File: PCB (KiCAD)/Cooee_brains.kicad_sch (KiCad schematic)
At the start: 35 parts, among them J1 USB4105-GF-A, J2 Conn_Coaxial, J3 503398-1892, J4 Conn_01x14_Socket, J5 Conn_02x20_Counter_Clockwise, J6 Conn_Coaxial, J7 Conn_01x04_Pin, J8 503480-1800, J9 Conn_01x18_Socket, SW1 Prog, SW2 Reset, U1 AMS1117-3.3, U2 ESP32-S3-WROOM-1-N8, U3 MAX98357AETE_T, U4 SX1262IMLTRT

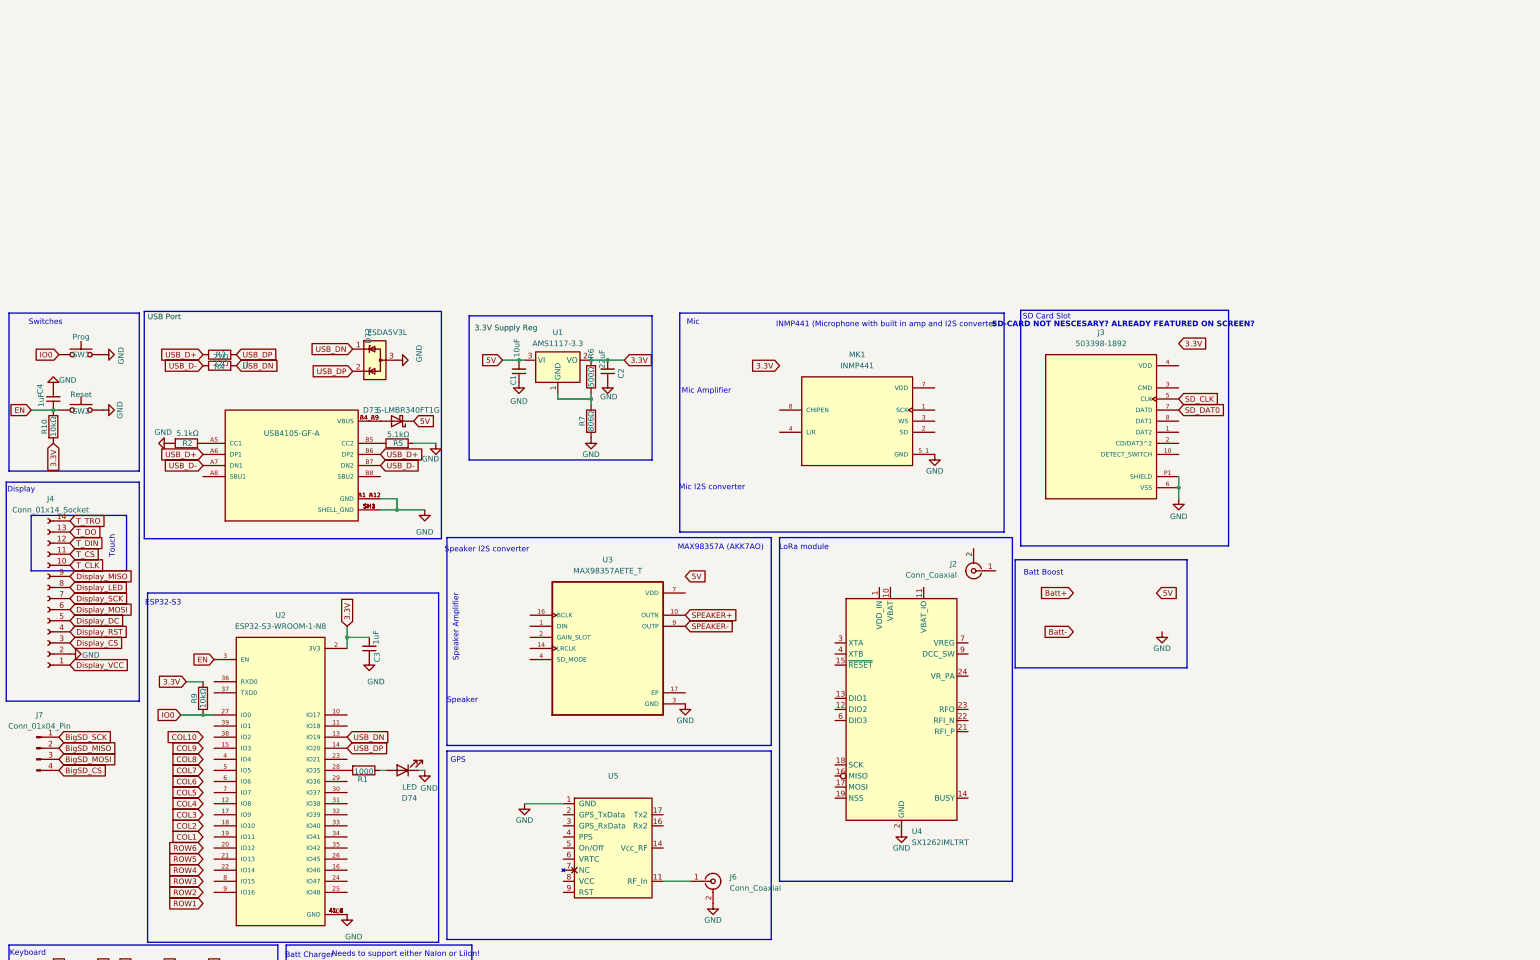
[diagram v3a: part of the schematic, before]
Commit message: swapped out complex SX1262 circuitry for a module
swapped out complex SX1262 circuitry for a module
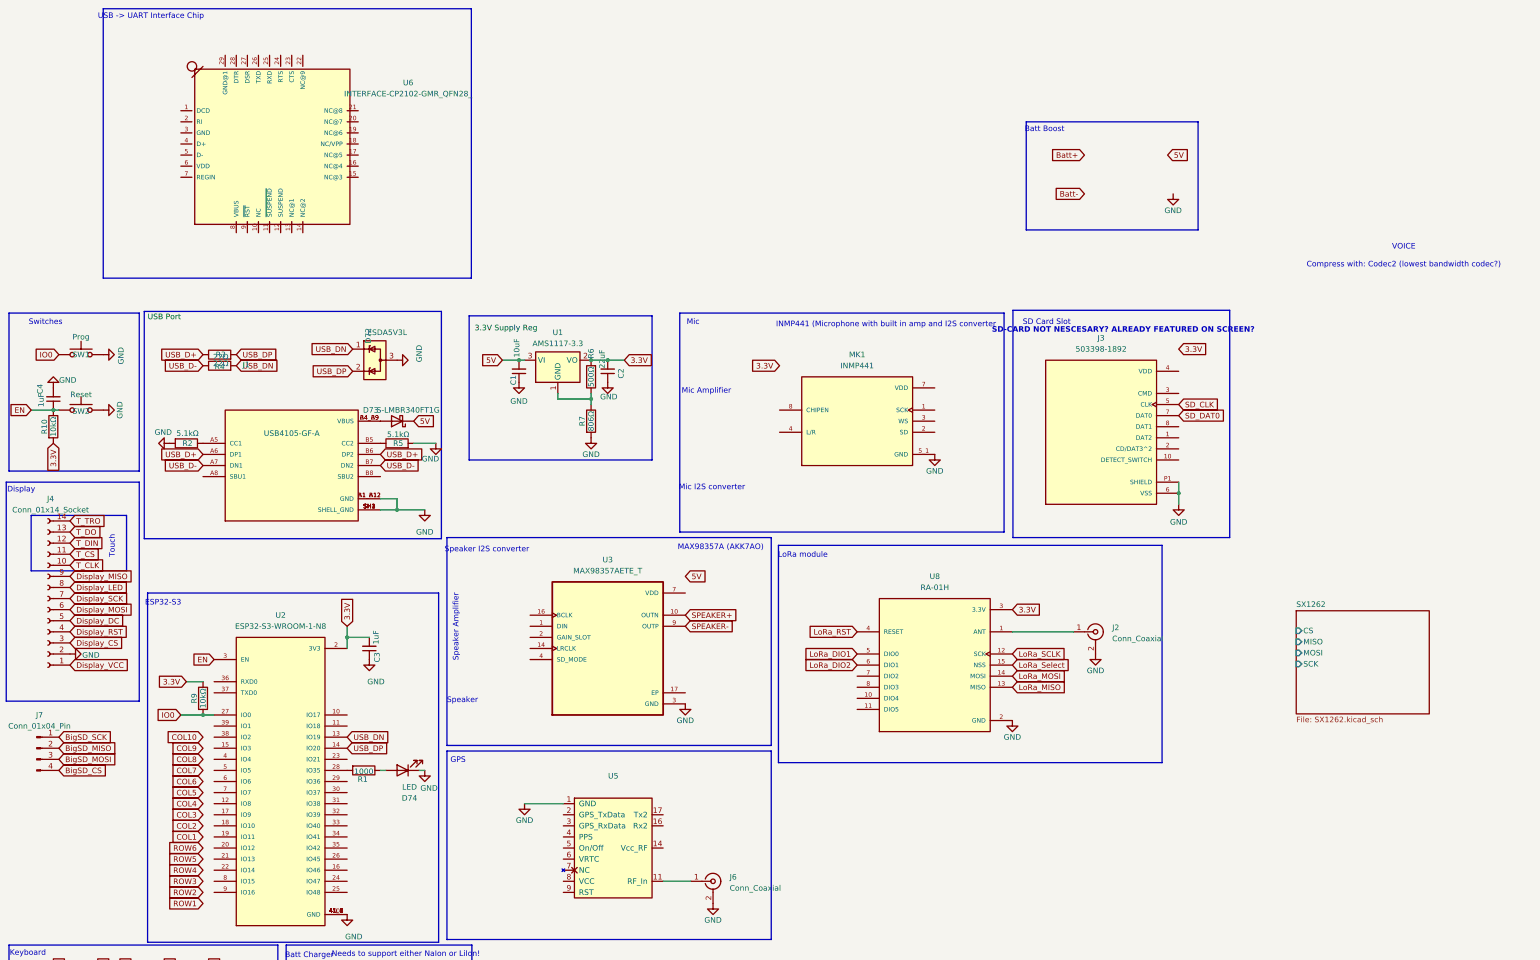
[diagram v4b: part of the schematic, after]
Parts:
- removed U4: SX1262IMLTRT, Package_DFN_QFN:QFN-24-1EP_4x4mm_P0.5mm_EP2.6x2.6mm, symbol RF:SX1262IMLTRT
- added U6: INTERFACE-CP2102-GMR_QFN28_, USB4105-GF-A (1):QFN28G_0.5-5X5MM, symbol Downloaded:INTERFACE-CP2102-GMR_QFN28_
- added U8: RA-01H, RF_Module:Ai-Thinker-Ra-01-LoRa, symbol Downloaded:RA-01H
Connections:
- net 3.3V: now also U8.3 (3.3V)
- net GND: now also J2.2 (Ext), U8.16 (GND), U8.2 (GND), U8.9 (GND)
- net at J2.1 (In): now also U8.1 (ANT)
- new net LoRa_DIO1: U8.5 (DIO0)
- new net LoRa_DIO2: U8.6 (DIO1)
- new net LoRa_MISO: U8.13 (MISO)
- new net LoRa_MOSI: U8.14 (MOSI)
- new net LoRa_RST: U8.4 (RESET)
- new net LoRa_SCLK: U8.12 (SCK)
- new net LoRa_Select: U8.15 (NSS)
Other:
- added sheet SX1262 (SX1262.kicad_sch)
- note added: "USB -> UART Interface Chip"
- note added: "VOICE Compress with: Codec2 (lowest bandwidth codec?)"
- moved on the sheet: J2, J3

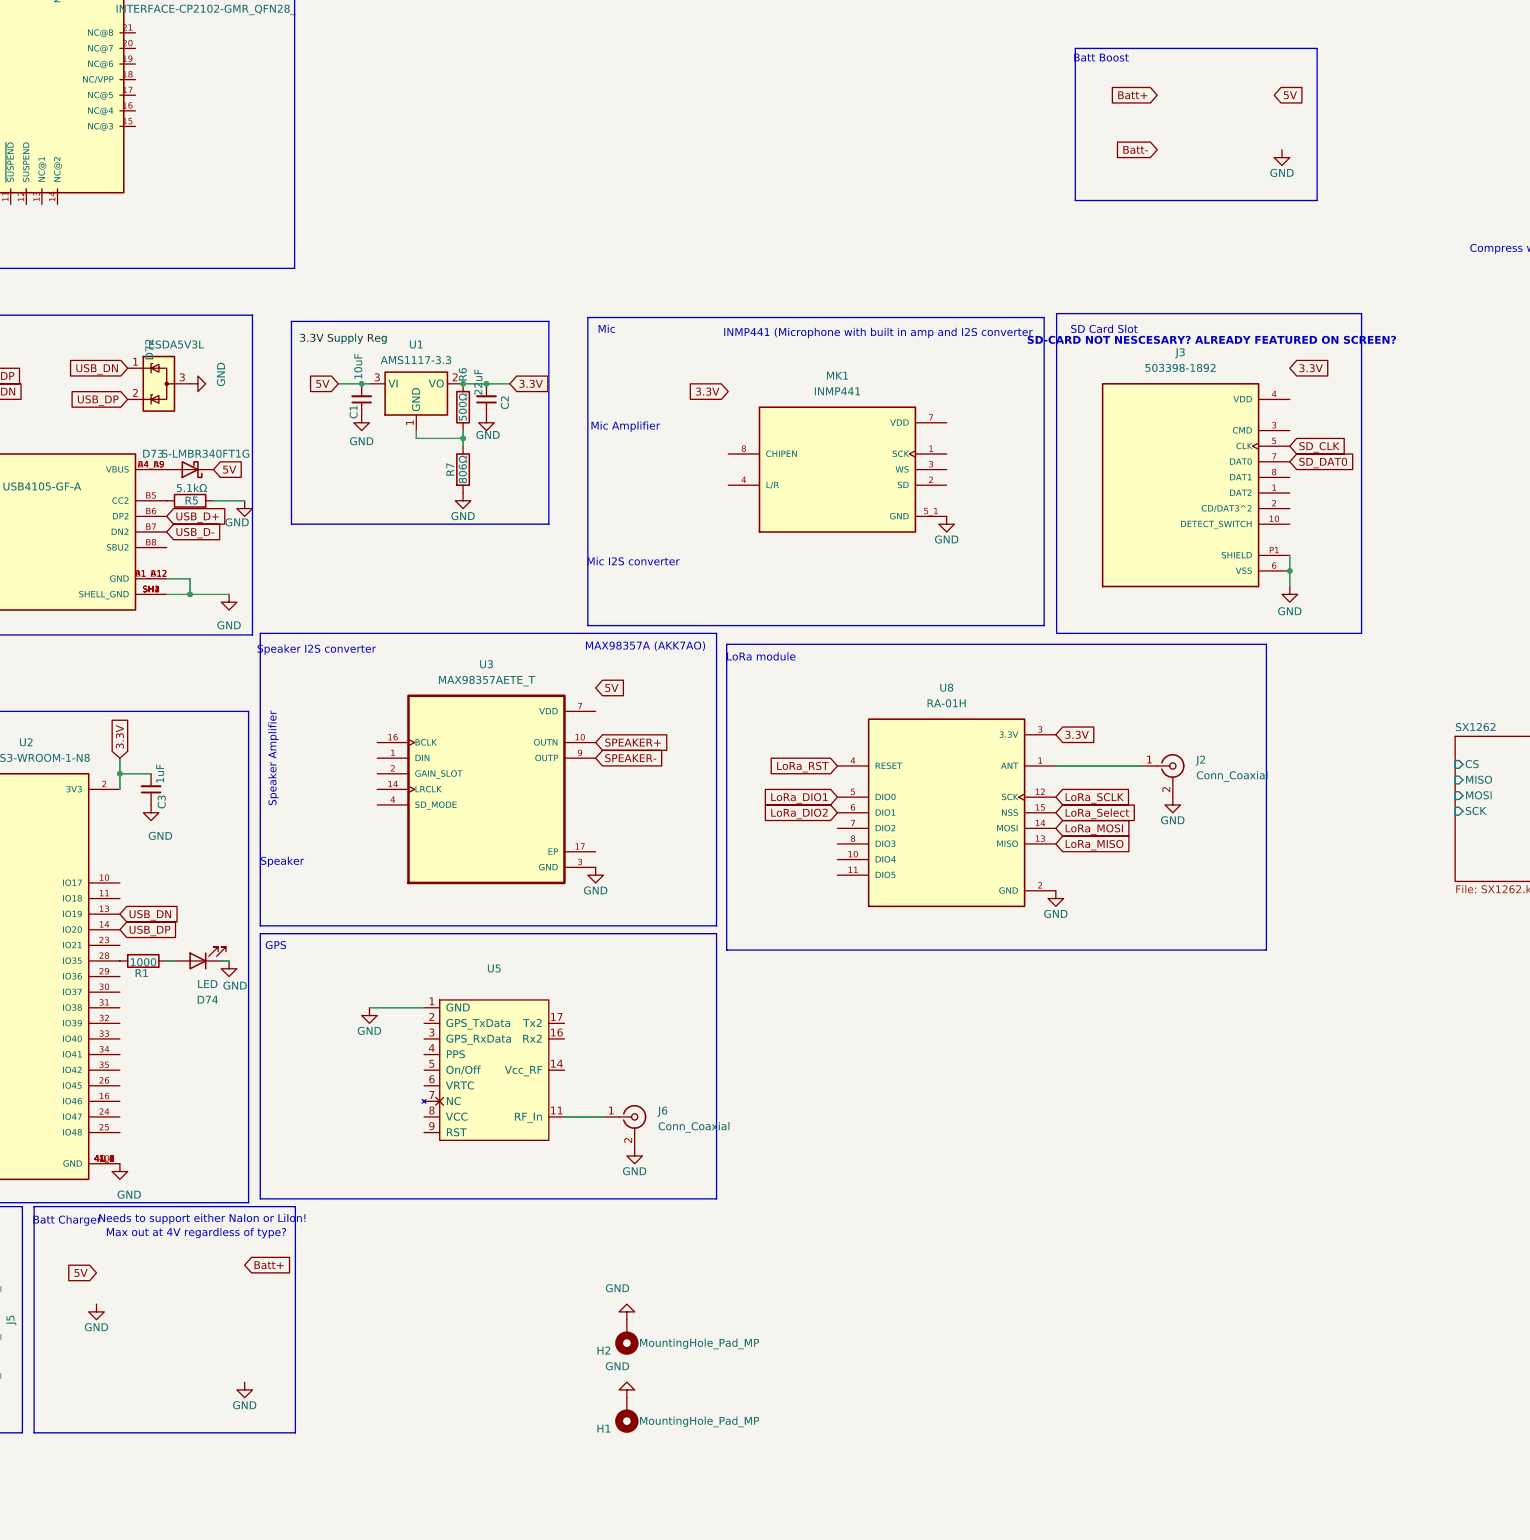
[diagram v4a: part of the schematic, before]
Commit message: more PCB work
should have the 90 degree SMD header pins lined up to mount now, unfortunately I've invalidated the keyboard prototypes I already bought
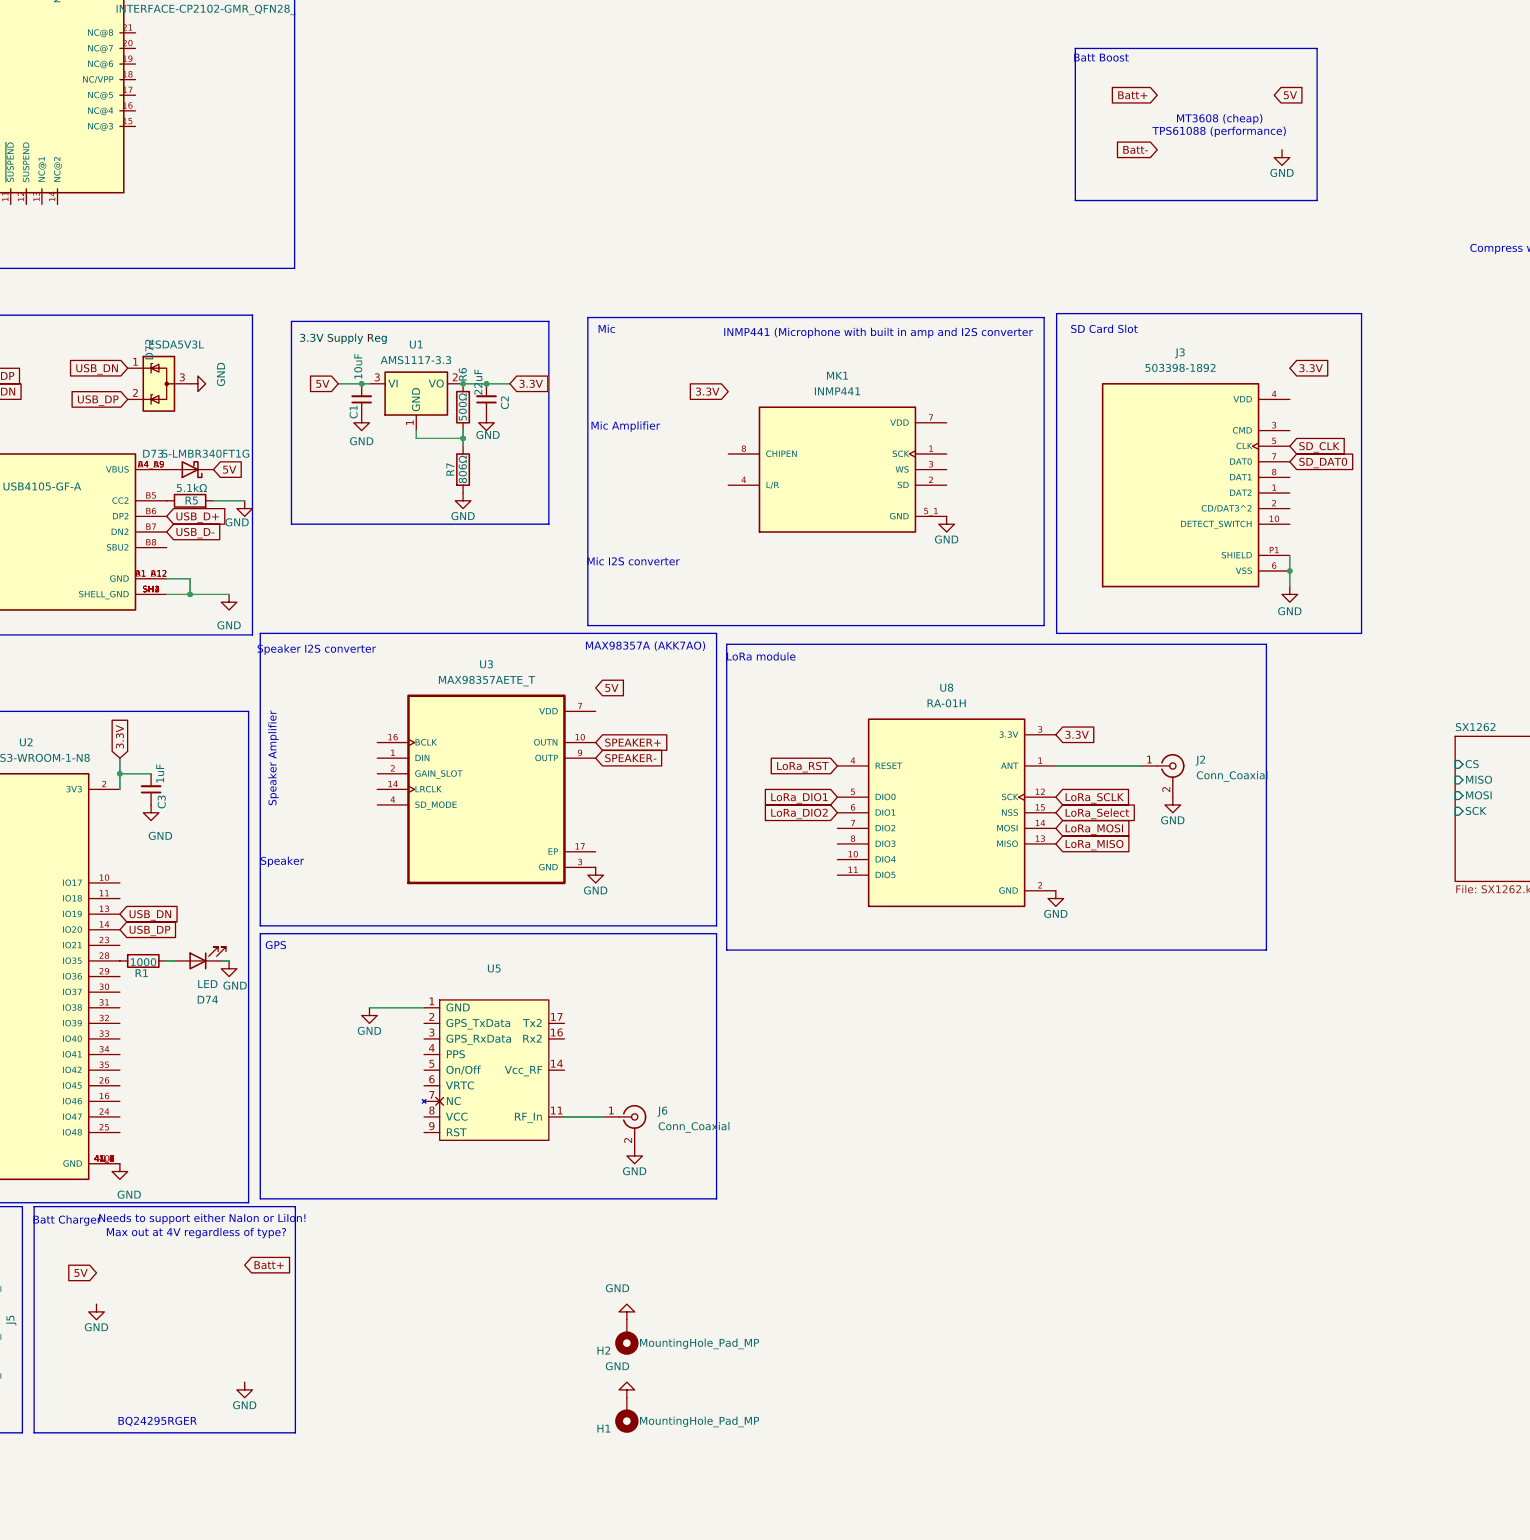
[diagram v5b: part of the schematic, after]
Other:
- note added: "BQ24295RGER"
- note added: "MT3608 (cheap) TPS61088 (performance)"
- note removed: "SD-CARD NOT NESCESARY? ALREADY FEATURED ON SCREEN?"
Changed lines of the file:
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@@
+		)
+	)
+	(text "MT3608 (cheap)\nTPS61088 (performance)"
+		(exclude_from_sim no)
+		(at 270.51 -16.51 0)
+		(effects
+			(font
+				(size 1.27 1.27)
+			)
 		)
 	)
@@
 		)
 	)
+	(text "BQ24295RGER\n"
+		(exclude_from_sim no)
+		(at 97.536 194.564 0)
+		(effects
+			(font
+				(size 1.27 1.27)
+			)
+		)
+	)
 	(text "Batt Charger"
 		(exclude_from_sim no)
@@
 			)
 		)
-	)
-	(text "SD-CARD NOT NESCESARY? ALREADY FEATURED ON SCREEN?"
-		(exclude_from_sim no)
-		(at 269.24 18.542 0)
-		(effects
-			(font
-				(size 1.27 1.27)
-				(thickness 0.254)
-				(bold yes)
-			)
-		)

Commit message: new IC choices for GPS, audio and power
also added a keyboard IC to the keyboard to preventing wasting precious ESP32 GPIOs
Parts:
- removed J5: Conn_02x20_Counter_Clockwise, Connector_PinHeader_2.54mm:PinHeader_2x20_P2.54mm_Vertical_SMD, symbol Connector_Generic:Conn_02x20_Counter_Clockwise
- removed J8: 503480-1800, USB4105-GF-A (1):MOLEX_503480-1800, symbol Downloaded:503480-1800
- removed J9: Conn_01x18_Socket, Connector_PinSocket_2.54mm:PinSocket_1x18_P2.54mm_Vertical_SMD_Pin1Left, symbol Connector:Conn_01x18_Socket
- added J5: Conn_01x02_Pin, Connector_PinHeader_2.54mm:PinHeader_1x02_P2.54mm_Horizontal, symbol Connector:Conn_01x02_Pin
- added J9: Conn_01x05_Socket, Connector_PinSocket_2.54mm:PinSocket_1x05_P2.54mm_Horizontal, symbol Connector:Conn_01x05_Socket
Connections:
- net Display_LED is gone; now on net Display_LED_BacklightEN: J4.8 (Pin_8)
- net Display_VCC is gone; now on net 3.3V: J4.1 (Pin_1)
- net T_DIN is gone; now on net T_MOSI: J4.12 (Pin_12)
- net T_DO is gone; now on net T_MISO: J4.13 (Pin_13)
- net T_TRO is gone; now on net T_IRQ: J4.14 (Pin_14)
- net 3.3V: now also J9.4 (Pin_4)
- net Display_CS: now also U2.5 (IO5)
- net Display_DC: now also U2.7 (IO7)
- net Display_MISO: now also U2.19 (IO11)
- net Display_MOSI: now also U2.12 (IO8)
- net Display_RST: now also U2.6 (IO6)
- net Display_SCK: now also U2.17 (IO9)
- net GND: now also U6.29 (GND@1), U6.3 (GND), J9.5 (Pin_5)
- net LoRa_MISO: now also U2.25 (IO48)
- net LoRa_MOSI: now also U2.24 (IO47)
- net LoRa_SCLK: now also U2.26 (IO45)
- net LoRa_Select: now also U2.16 (IO46)
- net SPEAKER+: now also J5.1 (Pin_1)
- net SPEAKER-: now also J5.2 (Pin_2)
- net T_CLK: now also U2.20 (IO12)
- net T_CS: now also U2.21 (IO13)
- net USB_D+: now also U6.4 (D+)
- net USB_D-: now also U6.5 (D-)
- net KEEB_SCL: now reaches U2.15 (IO3)
- net KEEB_SCL: now also J9.2 (Pin_2)
- net Display_LED_BacklightEN: now reaches U2.18 (IO10)
- net T_MOSI: now reaches U2.22 (IO14)
- net SHARED_MOSI: now reaches U2.29 (IO36)
- net SHARED_MISO: now reaches U2.30 (IO37)
- net SHARED_CLCK: now reaches U2.31 (IO38)
- net KEEP_RST: now reaches U2.38 (IO2)
- net KEEP_RST: now also J9.1 (Pin_1)
- net KEEB_D: now reaches U2.4 (IO4)
- net KEEB_D: now also J9.3 (Pin_3)
- net T_MISO: now reaches U2.8 (IO15)
- net T_IRQ: now reaches U2.9 (IO16)
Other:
- removed sheet SX1262
- note added: "LoRa Radio"
- note added: "SD_Card"
- note added: "Screen"
- note added: "USB"
- note removed: "VOICE Compress with: Codec2 (lowest bandwidth codec?)"
- moved on the sheet: C3, D74, J4, J7, R1, R9, U2, U6
